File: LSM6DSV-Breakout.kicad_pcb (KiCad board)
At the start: 2 copper layers, 16.5 x 20.3 mm, 16 parts, among them CN1 AFC10-S04QCA-00, CN2 AFC10-S04QCA-00, J1 Conn_01x06_Pin, J2 Conn_01x04_Pin, U1 LSM6DSVTR

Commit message: add heading mark
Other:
- board text added: "X"
- board text added: "Y"
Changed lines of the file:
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@@
+	)
+	(gr_line
+		(start 63.246 45.339)
+		(end 63.246 46.355)
+		(stroke
+			(width 0.1)
+			(type default)
+		)
+		(layer "F.SilkS")
+	)
+	(gr_line
+		(start 63.246 46.355)
+		(end 62.23 46.355)
+		(stroke
+			(width 0.1)
+			(type default)
+		)
+		(layer "F.SilkS")
 	)
 	(gr_line
@@
 		)
 	)
+	(gr_text "Y"
+		(at 61.722 46.355 90)
+		(layer "F.SilkS")
+		(effects
+			(font
+				(size 0.6 0.6)
+				(thickness 0.08)
+			)
+		)
+	)
 	(gr_text "G"
 		(at 54.356 46.736 270)
@@
 			)
 		)
+	)
+	(gr_text "X"
+		(at 63.246 45.085 90)
+		(layer "F.SilkS")
+		(effects
+			(font
+				(size 0.6 0.6)
+				(thickness 0.08)
+			)
+		)

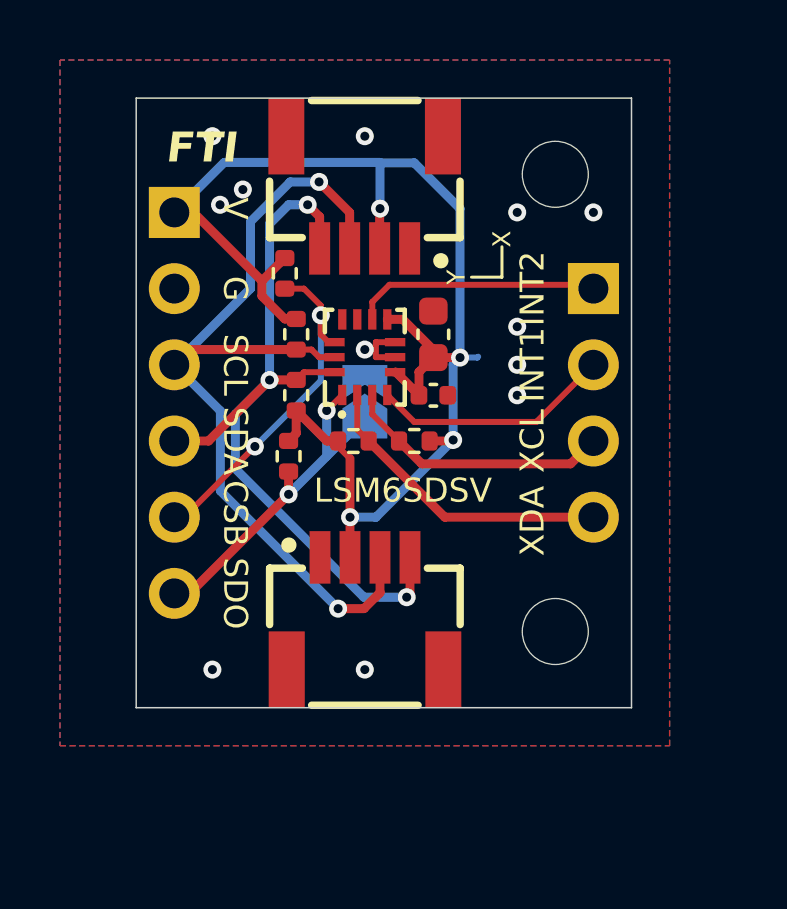
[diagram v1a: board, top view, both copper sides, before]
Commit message: Unified 6DoF IMU footprint
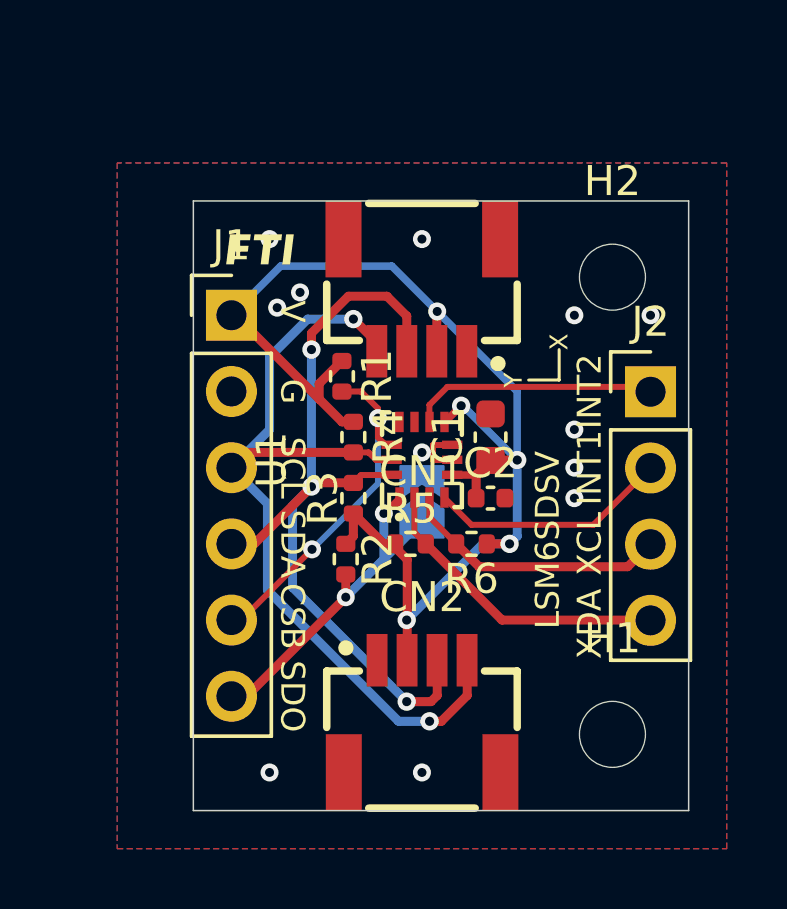
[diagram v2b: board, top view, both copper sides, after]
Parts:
- J1, J2: moved to F.Cu
- moved H1 18.8 mm to (66.9, 61.6)
- moved H2 12.0 mm to (66.9, 46.4)
- moved J2 3.93 mm to (68.2, 50.2), turned to 0 degrees
- moved R3 3.93 mm to (58.3, 53.7)
- moved R1 3.92 mm to (57.9, 49.7)
- moved C1 3.92 mm to (62.9, 51.7)
- moved CN1 3.92 mm to (60.6, 47.0)
- moved J1 3.92 mm to (54.2, 47.6), turned to 0 degrees
- moved R2 3.92 mm to (58.0, 55.8)
- moved C2 3.92 mm to (62.9, 53.7)
- moved R4 3.92 mm to (58.3, 51.7)
- moved R6 3.92 mm to (62.2, 55.2)
- moved R5 3.92 mm to (60.2, 55.2)
- moved CN2 3.92 mm to (60.6, 61.0)
- moved U1 3.91 mm to (60.6, 52.4)
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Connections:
- net VCC renamed VDD
- CN1 pad 3: /SCL -> /SDA
- CN1 pad 4: /SDA -> /SCL
- CN2 pad 3: /SCL -> /SDA
- CN2 pad 4: /SDA -> /SCL
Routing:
- net VDD: track 49.8 -> 45.6 mm, vias 4 -> 5
- net /SCL: track 30.1 -> 29.2 mm
- net /SDA: track 27.5 -> 28.4 mm
